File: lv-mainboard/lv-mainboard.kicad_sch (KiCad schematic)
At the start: 90 parts, among them J1 Conn_02x13_Odd_Even, J10 Power, J11 Power, J12 CAN, J13 CAN_Brake, J14 CAN_lvbms, J15 CAN, J16 SideBoard, J17 SideBoard, J18 SideBoard, J19 SideBoard, J2 Conn_02x10_Odd_Even, J20 SideBoard, J21 SideBoard, J22 SDC OUT, J23 SDC OUT, J24 Mainhoop-Light, J25 ACC, J26 ACC, J27 ACC_PWR, J28 ACC_PRW, J29 Power, J3 Conn_02x10_Odd_Even, J30 BSE, J31 Brake Light, J32 Brake Light, J33 BSE, J34 Power, J35 Power, J4 Conn_02x10_Odd_Even, J5 Power, J6 Power, J7 Power, J8 Power, J9 Power, U1 AP63200WU, U2 AP63200WU

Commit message: feat: lv-mainboard v2025.12
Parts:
- removed J29: Power, Connector_JST:JST_XH_S2B-XH-A-1_1x02_P2.50mm_Horizontal, symbol Connector_Generic:Conn_01x02
- added C13: 1u, Capacitor_SMD:C_0603_1608Metric, symbol Device:C_Small
- added C14: 10u, Capacitor_SMD:C_0805_2012Metric, symbol Device:C_Small
- added J29: ACC, Connector_JST:JST_XH_B4B-XH-A_1x04_P2.50mm_Vertical, symbol Connector_Generic:Conn_01x04
- added J36: 1-Temp1, Connector_JST:JST_XH_B3B-XH-A_1x03_P2.50mm_Vertical, symbol Connector_Generic:Conn_01x03
- added J37: 1-Temp2, Connector_JST:JST_XH_B3B-XH-A_1x03_P2.50mm_Vertical, symbol Connector_Generic:Conn_01x03
- added J38: 1-PUMP, Connector_JST:JST_XH_B3B-XH-A_1x03_P2.50mm_Vertical, symbol Connector_Generic:Conn_01x03
- added J39: 1-FAN, Connector_JST:JST_XH_B3B-XH-A_1x03_P2.50mm_Vertical, symbol Connector_Generic:Conn_01x03
- added J40: 1-Pressure, Connector_JST:JST_XH_B3B-XH-A_1x03_P2.50mm_Vertical, symbol Connector_Generic:Conn_01x03
- added J41: 1-Flow, Connector_JST:JST_XH_B3B-XH-A_1x03_P2.50mm_Vertical, symbol Connector_Generic:Conn_01x03
- added J42: 2-Temp1, Connector_JST:JST_XH_B3B-XH-A_1x03_P2.50mm_Vertical, symbol Connector_Generic:Conn_01x03
- added J43: 2-Temp2, Connector_JST:JST_XH_B3B-XH-A_1x03_P2.50mm_Vertical, symbol Connector_Generic:Conn_01x03
- added J44: 2-Pressure, Connector_JST:JST_XH_B3B-XH-A_1x03_P2.50mm_Vertical, symbol Connector_Generic:Conn_01x03
- added J45: 2-Flow, Connector_JST:JST_XH_B3B-XH-A_1x03_P2.50mm_Vertical, symbol Connector_Generic:Conn_01x03
- added J46: 2-PUMP, Connector_JST:JST_XH_B3B-XH-A_1x03_P2.50mm_Vertical, symbol Connector_Generic:Conn_01x03
- added J47: 2-FAN, Connector_JST:JST_XH_B3B-XH-A_1x03_P2.50mm_Vertical, symbol Connector_Generic:Conn_01x03
- added J48: ACC, Connector_JST:JST_XH_B2B-XH-A_1x02_P2.50mm_Vertical, symbol Connector_Generic:Conn_01x02
- added R16: 100k, Resistor_SMD:R_0603_1608Metric, symbol Device:R_Small
- added R17: 301k, Resistor_SMD:R_0603_1608Metric, symbol Device:R_Small
- added TP3: TestPoint, TestPoint:TestPoint_THTPad_D1.5mm_Drill0.7mm, symbol Connector:TestPoint
- added U3: AP2204K-ADJ, Package_TO_SOT_SMD:SOT-23-5, symbol Regulator_Linear:AP2204K-ADJ
- R14, R15: value R -> 150R
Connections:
- net +6V: now also C13.1, U3.1 (VIN), U3.3 (EN)
- net BMS_FAULT: now also J29.3 (Pin_3)
- net E1: now also J6.2 (Pin_2), J7.2 (Pin_2), J38.3 (Pin_3), J39.3 (Pin_3), J46.3 (Pin_3), J47.3 (Pin_3); no longer J6.1 (Pin_1), J7.1 (Pin_1)
- net E2: now also J5.2 (Pin_2); no longer J5.1 (Pin_1)
- net E3: now also J8.2 (Pin_2); no longer J8.1 (Pin_1)
- net FAN_PWM_1: now also J39.2 (Pin_2)
- net FAN_PWM_2: now also J47.2 (Pin_2)
- net GND: now also J10.1 (Pin_1), J11.1 (Pin_1), J34.1 (Pin_1), J35.1 (Pin_1), J5.1 (Pin_1), J6.1 (Pin_1), J7.1 (Pin_1), J8.1 (Pin_1), J9.1 (Pin_1), C13.2, C14.2, J29.1 (Pin_1), J36.1 (Pin_1), J37.1 (Pin_1), J38.1 (Pin_1), J39.1 (Pin_1), J40.1 (Pin_1), J41.1 (Pin_1), J42.1 (Pin_1), J43.1 (Pin_1), J44.1 (Pin_1), J45.1 (Pin_1), J46.1 (Pin_1), J47.1 (Pin_1), J48.1 (Pin_1), R16.1, U3.2 (GND); no longer J10.2 (Pin_2), J11.2 (Pin_2), J22.2 (Pin_2), J23.2 (Pin_2), J30.1 (Pin_1), J33.1 (Pin_1), J5.2 (Pin_2), J6.2 (Pin_2), J7.2 (Pin_2), J8.2 (Pin_2), J9.2 (Pin_2)
- net IMD_FAULT: now also J29.4 (Pin_4)
- net P2: now also J30.1 (Pin_1), J33.1 (Pin_1)
- net P5: now also J34.2 (Pin_2), J35.2 (Pin_2); no longer J34.1 (Pin_1), J35.1 (Pin_1)
- net P6: no longer J34.2 (Pin_2), J35.2 (Pin_2)
- net P7: now also J9.2 (Pin_2); no longer J9.1 (Pin_1)
- net P8: now also J10.2 (Pin_2); no longer J10.1 (Pin_1)
- net P9: now also J11.2 (Pin_2); no longer J11.1 (Pin_1)
- net PT_signal_1: now also J40.2 (Pin_2)
- net PT_signal_2: now also J44.2 (Pin_2)
- net PUMP_PWM_1: now also J38.2 (Pin_2)
- net PUMP_PWM_2: now also J46.2 (Pin_2)
- net SDC_OUT: now also J22.2 (Pin_2), J23.2 (Pin_2)
- net TIM1_CH1_1: now also J41.2 (Pin_2)
- net TIM1_CH1_2: now also J45.2 (Pin_2)
- net TSAL: now also J29.2 (Pin_2)
- net USART1_1: now also J36.2 (Pin_2)
- net USART1_2: now also J42.2 (Pin_2)
- net USART2_1: now also J37.2 (Pin_2)
- net USART2_2: now also J43.2 (Pin_2)
- net current_init: now also J48.2 (Pin_2)
- new net: R16.2, R17.2, U3.4 (ADJ)
- new net +5V: C14.1, J36.3 (Pin_3), J37.3 (Pin_3), J40.3 (Pin_3), J41.3 (Pin_3), J42.3 (Pin_3), J43.3 (Pin_3), J44.3 (Pin_3), J45.3 (Pin_3), R17.1, TP3.1, U3.5 (VOUT)
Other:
- note added: "4mA -> 0.6V 20mV-> 3V"
- note added: "LDO"
- note added: "LV(15V & 6V & 5V)"
- note added: "LV11"
- note added: "LV12"
- note added: "LV13"
- note added: "LV14"
- note removed: "LV(15V & 6V)"
- moved on the sheet: C1, C10, C11, C12, C2, C3, C4, C5, C6, C7, C8, C9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

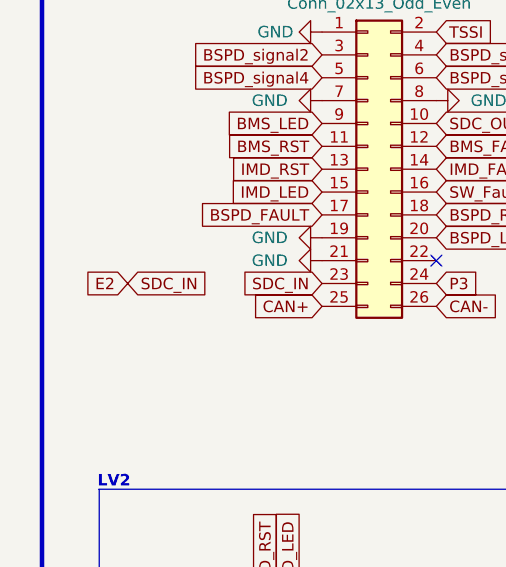
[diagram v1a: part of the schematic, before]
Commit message: modify: replace SDC pwr with P8
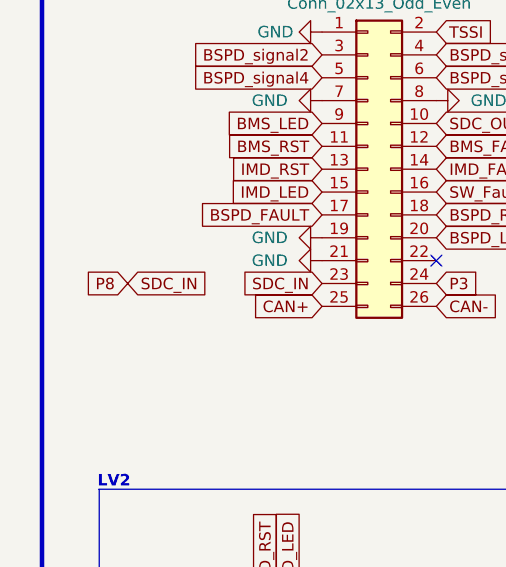
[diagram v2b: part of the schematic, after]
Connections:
- net E2: no longer J1.23 (Pin_23)
- net P8: now also J1.23 (Pin_23)
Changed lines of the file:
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@@
+		)
+	)
+	(global_label "P8"
+		(shape input)
+		(at 33.02 193.04 180)
+		(fields_autoplaced yes)
+		(effects
+			(font
+				(size 1.27 1.27)
+			)
+			(justify right)
+		)
+		(property "Intersheetrefs" "${INTERSHEET_REFS}"
+			(at 27.5553 193.04 0)
+			(effects
+				(font
+					(size 1.27 1.27)
+				)
+				(justify right)
+				(hide yes)
+			)
 		)
 	)
@@
 				(hide yes)
 			)
-		)
-	)
-	(global_label "E2"
-		(shape input)
-		(at 33.02 193.04 180)
-		(fields_autoplaced yes)
-		(effects
-			(font
-				(size 1.27 1.27)
-				(color 0 255 255 1)
-			)
-			(justify right)
-		)
-		(property "Intersheetrefs" "${INTERSHEET_REFS}"
-			(at 27.6763 193.04 0)
-			(effects
-				(font
-					(size 1.27 1.27)
-				)
-				(justify right)
-				(hide yes)
-			)
